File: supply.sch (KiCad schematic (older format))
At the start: 35 parts

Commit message: - battery charger develop - added sheet (every sheet contains total number of sheets, thats beacouse here are changes in all sheets)
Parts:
- removed C? (x6): 1u, symbol Device:C_Small
- removed D? (x2): D_Small, symbol Device:D_Small
- added C? (x6): 1u, Capacitor_SMD:C_0603_1608Metric_Pad1.05x0.95mm_HandSolder, symbol Device:C_Small
- added C? (x4): 2u2, Capacitor_SMD:C_0805_2012Metric_Pad1.15x1.40mm_HandSolder, symbol Device:C_Small
- added D? (x2): PMEG4005EJ, Diode_SMD:D_SOD-323F, symbol Diode:PMEG4005EJ
- added D?: Green, Diode_SMD:D_0805_2012Metric_Pad1.15x1.40mm_HandSolder, symbol Device:LED_Small
- added D?: Red, Diode_SMD:D_0805_2012Metric_Pad1.15x1.40mm_HandSolder, symbol Device:LED_Small
- added NTC?: 10k, Resistor_THT:R_Axial_DIN0204_L3.6mm_D1.6mm_P2.54mm_Vertical, symbol Device:Thermistor_NTC
- added Q?: BC807, Package_TO_SOT_SMD:SOT-23, symbol Transistor_BJT:BC807
- added Q?: BC817, Package_TO_SOT_SMD:SOT-23, symbol Device:Q_NPN_BCE
- added Q? (x2): BSS138, Package_TO_SOT_SMD:SOT-23, symbol Transistor_FET:BSS138
- added R?: 10k, Resistor_SMD:R_0603_1608Metric_Pad1.05x0.95mm_HandSolder, symbol Device:R_Small
- added R? (x4): 47k, Resistor_SMD:R_0603_1608Metric_Pad1.05x0.95mm_HandSolder, symbol Device:R_Small
- added R?: 1k3, Resistor_SMD:R_0603_1608Metric_Pad1.05x0.95mm_HandSolder, symbol Device:R_Small
- added R?: 890R, Resistor_SMD:R_0603_1608Metric_Pad1.05x0.95mm_HandSolder, symbol Device:R_Small
- added R? (x3): 1k, Resistor_SMD:R_0603_1608Metric_Pad1.05x0.95mm_HandSolder, symbol Device:R_Small
- added SW?: SW_DIP_x02, Button_Switch_SMD:SW_DIP_SPSTx02_Slide_6.7x6.64mm_W8.61mm_P2.54mm_LowProfile, symbol Switch:SW_DIP_x02
- added SW?: PWRON, symbol Switch:SW_MEC_5E
- C? (x4): footprint (none) -> Capacitor_SMD:C_0603_1608Metric_Pad1.05x0.95mm_HandSolder
- D?: footprint (none) -> Diode_SMD:D_0805_2012Metric_Pad1.15x1.40mm_HandSolder
- R? (x8): footprint (none) -> Resistor_SMD:R_0603_1608Metric_Pad1.05x0.95mm_HandSolder
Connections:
- net labels added: PWRON_MCU, SYSOFF, Vusb
- wire segments 77 -> 136
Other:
- note added: "PMEG4005 - Ir = 8 uA, surge 10 A\nCd = 43 pF - that is, @12V 500 kHz -> W = 6.2nJ, P = 3 mW\nPMEG4005EJ - 5 Aavg"
- moved on the sheet: BT?, C?, D?, J?, R?, U?

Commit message: - supply converter develop - added sheet: MCU - cleanup 'koncepcja' sub-schematics
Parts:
- removed BT?: Battery_Cell, symbol Device:Battery_Cell
- removed C? (x6): 1u, Capacitor_SMD:C_0603_1608Metric_Pad1.05x0.95mm_HandSolder, symbol Device:C_Small
- removed C? (x4): 2u2, Capacitor_SMD:C_0805_2012Metric_Pad1.15x1.40mm_HandSolder, symbol Device:C_Small
- removed D?: Orange, Diode_SMD:D_0805_2012Metric_Pad1.15x1.40mm_HandSolder, symbol Device:LED_Small
- removed D?: Green, Diode_SMD:D_0805_2012Metric_Pad1.15x1.40mm_HandSolder, symbol Device:LED_Small
- removed D?: Red, Diode_SMD:D_0805_2012Metric_Pad1.15x1.40mm_HandSolder, symbol Device:LED_Small
- removed J?: USB_B_Micro, Connector_USB:USB_Micro-B_Amphenol_10103594-0001LF_Horizontal, symbol Connector:USB_B_Micro
- removed NTC?: 10k, Resistor_THT:R_Axial_DIN0204_L3.6mm_D1.6mm_P2.54mm_Vertical, symbol Device:Thermistor_NTC
- removed Q? (x2): SI2365EDS, Package_TO_SOT_SMD:SOT-23, symbol Device:Q_PMOS_GDS
- removed Q? (x2): BC817, Package_TO_SOT_SMD:SOT-23, symbol Device:Q_NPN_BCE
- removed Q?: BC807, Package_TO_SOT_SMD:SOT-23, symbol Transistor_BJT:BC807
- removed Q? (x2): BSS138, Package_TO_SOT_SMD:SOT-23, symbol Transistor_FET:BSS138
- removed R? (x3): 10k, Resistor_SMD:R_0603_1608Metric_Pad1.05x0.95mm_HandSolder, symbol Device:R_Small
- removed R? (x5): 1k, Resistor_SMD:R_0603_1608Metric_Pad1.05x0.95mm_HandSolder, symbol Device:R_Small
- removed R? (x4): 47k, Resistor_SMD:R_0603_1608Metric_Pad1.05x0.95mm_HandSolder, symbol Device:R_Small
- removed R?: 1k3, Resistor_SMD:R_0603_1608Metric_Pad1.05x0.95mm_HandSolder, symbol Device:R_Small
- removed R?: 890R, Resistor_SMD:R_0603_1608Metric_Pad1.05x0.95mm_HandSolder, symbol Device:R_Small
- removed SW?: SW_DIP_x02, Button_Switch_SMD:SW_DIP_SPSTx02_Slide_6.7x6.64mm_W8.61mm_P2.54mm_LowProfile, symbol Switch:SW_DIP_x02
- removed SW?: PWRON, symbol Switch:SW_MEC_5E
- removed U?: BQ24079RGT, Package_DFN_QFN:VQFN-16-1EP_3x3mm_P0.5mm_EP1.6x1.6mm, symbol Battery_Management:BQ24079RGT
- added C? (x5): 2u2, Capacitor_SMD:C_0805_2012Metric_Pad1.15x1.40mm_HandSolder, symbol Device:C_Small
- added C? (x5): 1u, Capacitor_SMD:C_0603_1608Metric_Pad1.05x0.95mm_HandSolder, symbol Device:C_Small
- added C?: 1u, Capacitor_SMD:C_0805_2012Metric_Pad1.15x1.40mm_HandSolder, symbol Device:C_Small
- added C? (x6): 100n, Capacitor_SMD:C_0603_1608Metric_Pad1.05x0.95mm_HandSolder, symbol Device:C_Small
- added D? (x2): PMEG4005EJ, Diode_SMD:D_SOD-323F, symbol Diode:PMEG4005EJ
- added D? (x4): 1N4448, Diode_SMD:D_SOD-323_HandSoldering, symbol Device:D_Small
- added R?: 1R, Resistor_SMD:R_0603_1608Metric_Pad1.05x0.95mm_HandSolder, symbol Device:R_Small
- added U?: L78L05_SO8, Package_SO:SOIC-8_3.9x4.9mm_P1.27mm, symbol Regulator_Linear:L78L05_SO8
- added U?: L79L05_SO8, Package_SO:SOIC-8_3.9x4.9mm_P1.27mm, symbol Regulator_Linear:L79L05_SO8
- C?: footprint Capacitor_SMD:C_0603_1608Metric_Pad1.05x0.95mm_HandSolder -> Capacitor_SMD:C_0805_2012Metric_Pad1.15x1.40mm_HandSolder
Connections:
- net labels added: +5V, -5V, BATT_IN
- net labels removed: +BATT, HV_EN, PWRON_MCU, SYSOFF, Vusb
- wire segments 136 -> 98
- no-connect marks 3 -> 0
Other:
- note added: "PMEG4005 - Ir = 8 uA, surge 10 A\nCd = 43 pF - that is, @12V 500 kHz -> W = 6.2nJ, P = 3 mW\n\nPMEG4005EJ - 5 Aavg"
- note removed: "PMEG4005 - Ir = 8 uA, surge 10 A\nCd = 43 pF - that is, @12V 500 kHz -> W = 6.2nJ, P = 3 mW\nPMEG4005EJ - 5 Aavg"
- moved on the sheet: C?, D?, L?, R?

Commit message: - added footprint & 3D model of DC/DC HV converter - updated battery (to 2x battery holder) - some changes in supply
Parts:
- removed C?: 2u2, Capacitor_SMD:C_0805_2012Metric_Pad1.15x1.40mm_HandSolder, symbol Device:C_Small
- removed C?: 100n, Capacitor_SMD:C_0603_1608Metric_Pad1.05x0.95mm_HandSolder, symbol Device:C_Small
- removed C? (x3): 1u, Capacitor_SMD:C_0603_1608Metric_Pad1.05x0.95mm_HandSolder, symbol Device:C_Small
- removed D? (x3): 1N4448, Diode_SMD:D_SOD-323_HandSoldering, symbol Device:D_Small
- removed D? (x4): PMEG4005EJ, Diode_SMD:D_SOD-323F, symbol Diode:PMEG4005EJ
- removed U?: L78L15_SO8, Package_SO:SOIC-8_3.9x4.9mm_P1.27mm, symbol Regulator_Linear:L78L15_SO8
- removed U?: PAM242x, Package_SO:SOIC-8-1EP_3.9x4.9mm_P1.27mm_EP2.29x3mm_ThermalVias, symbol Diotec:PAM242x
- removed U?: L78L05_SO8, Package_SO:SOIC-8_3.9x4.9mm_P1.27mm, symbol Regulator_Linear:L78L05_SO8
- removed U?: L79L05_SO8, Package_SO:SOIC-8_3.9x4.9mm_P1.27mm, symbol Regulator_Linear:L79L05_SO8
- added C? (x3): 1u, Capacitor_SMD:C_0603_1608Metric_Pad1.05x0.95mm_HandSolder, symbol Device:C_Small
- added C?: 1u, Capacitor_SMD:C_0805_2012Metric_Pad1.15x1.40mm_HandSolder, symbol Device:C_Small
- added C?: 2u2, Capacitor_SMD:C_0805_2012Metric_Pad1.15x1.40mm_HandSolder, symbol Device:C_Small
- added C? (x2): 100n, Capacitor_SMD:C_0603_1608Metric_Pad1.05x0.95mm_HandSolder, symbol Device:C_Small
- added C?: 1n, Capacitor_SMD:C_0805_2012Metric_Pad1.15x1.40mm_HandSolder, symbol Device:C_Small
- added C? (x4): 10u, Capacitor_SMD:C_0805_2012Metric_Pad1.15x1.40mm_HandSolder, symbol Device:C_Small
- added D?: 1N4448, Diode_SMD:D_SOD-323_HandSoldering, symbol Device:D_Small
- added D? (x6): PMEG4005EJ, Diode_SMD:D_SOD-323_HandSoldering, symbol Diode:PMEG4005EJ
- added D?: PMEG4005EJ, Diode_SMD:D_SOD-123F, symbol Diode:PMEG4005EJ
- added L?: 2u2, Inductor_SMD:L_1008_2520Metric, symbol Device:L_Core_Ferrite
- added R?: 13k2, Resistor_SMD:R_0603_1608Metric_Pad1.05x0.95mm_HandSolder, symbol Device:R_Small
- added R? (x2): 1k2, Resistor_SMD:R_0603_1608Metric_Pad1.05x0.95mm_HandSolder, symbol Device:R_Small
- added R?: 1R, Resistor_SMD:R_0603_1608Metric_Pad1.05x0.95mm_HandSolder, symbol Device:R_Small
- added R?: 3k6, Resistor_SMD:R_0603_1608Metric_Pad1.05x0.95mm_HandSolder, symbol Device:R_Small
- added R?: 5R, Resistor_SMD:R_0603_1608Metric_Pad1.05x0.95mm_HandSolder, symbol Device:R_Small
- added U?: LM317L_SOT89, Package_TO_SOT_SMD:SOT-89-3, symbol Regulator_Linear:LM317L_SOT-89
- added U?: PAM242x, symbol DiodesInc:PAM242x
- added U?: LM337L_SO8, Package_SO:SOIC-8_3.9x4.9mm_P1.27mm, symbol Regulator_Linear:LM337L_SO8
- added U?: TPS613222ADBV, Package_TO_SOT_SMD:SOT-23-5, symbol Regulator_Switching:TPS613222ADBV
- D?: value PMEG60T50 -> PMEG3050BEP
- R?: value 10k -> 1k
- R?: value 85k -> 8k5
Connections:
- wire segments 98 -> 136
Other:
- note added: "PMEG4005 - Ir = 8 uA, surge 10 A\nCd = 43 pF - that is, @12V 500 kHz -> W = 6.2nJ, P = 3 mW\n\nPMEG4005EJ - 5 Aavg\n\n5 V line current: ca. 100-150 mA\n\nLM317/LM337 was used instead fixed LDO's beacouse of lower Iq (bias) current."
- note added: "Recommended 3x GRM188R60J106ME84D\n0603 10 uF 6.3V X5R 20% MLCC\n\nSnubber: C must be >3x diode capacitance"
- note removed: "PMEG4005 - Ir = 8 uA, surge 10 A\nCd = 43 pF - that is, @12V 500 kHz -> W = 6.2nJ, P = 3 mW\n\nPMEG4005EJ - 5 Aavg"
- moved on the sheet: C?, D?, R?

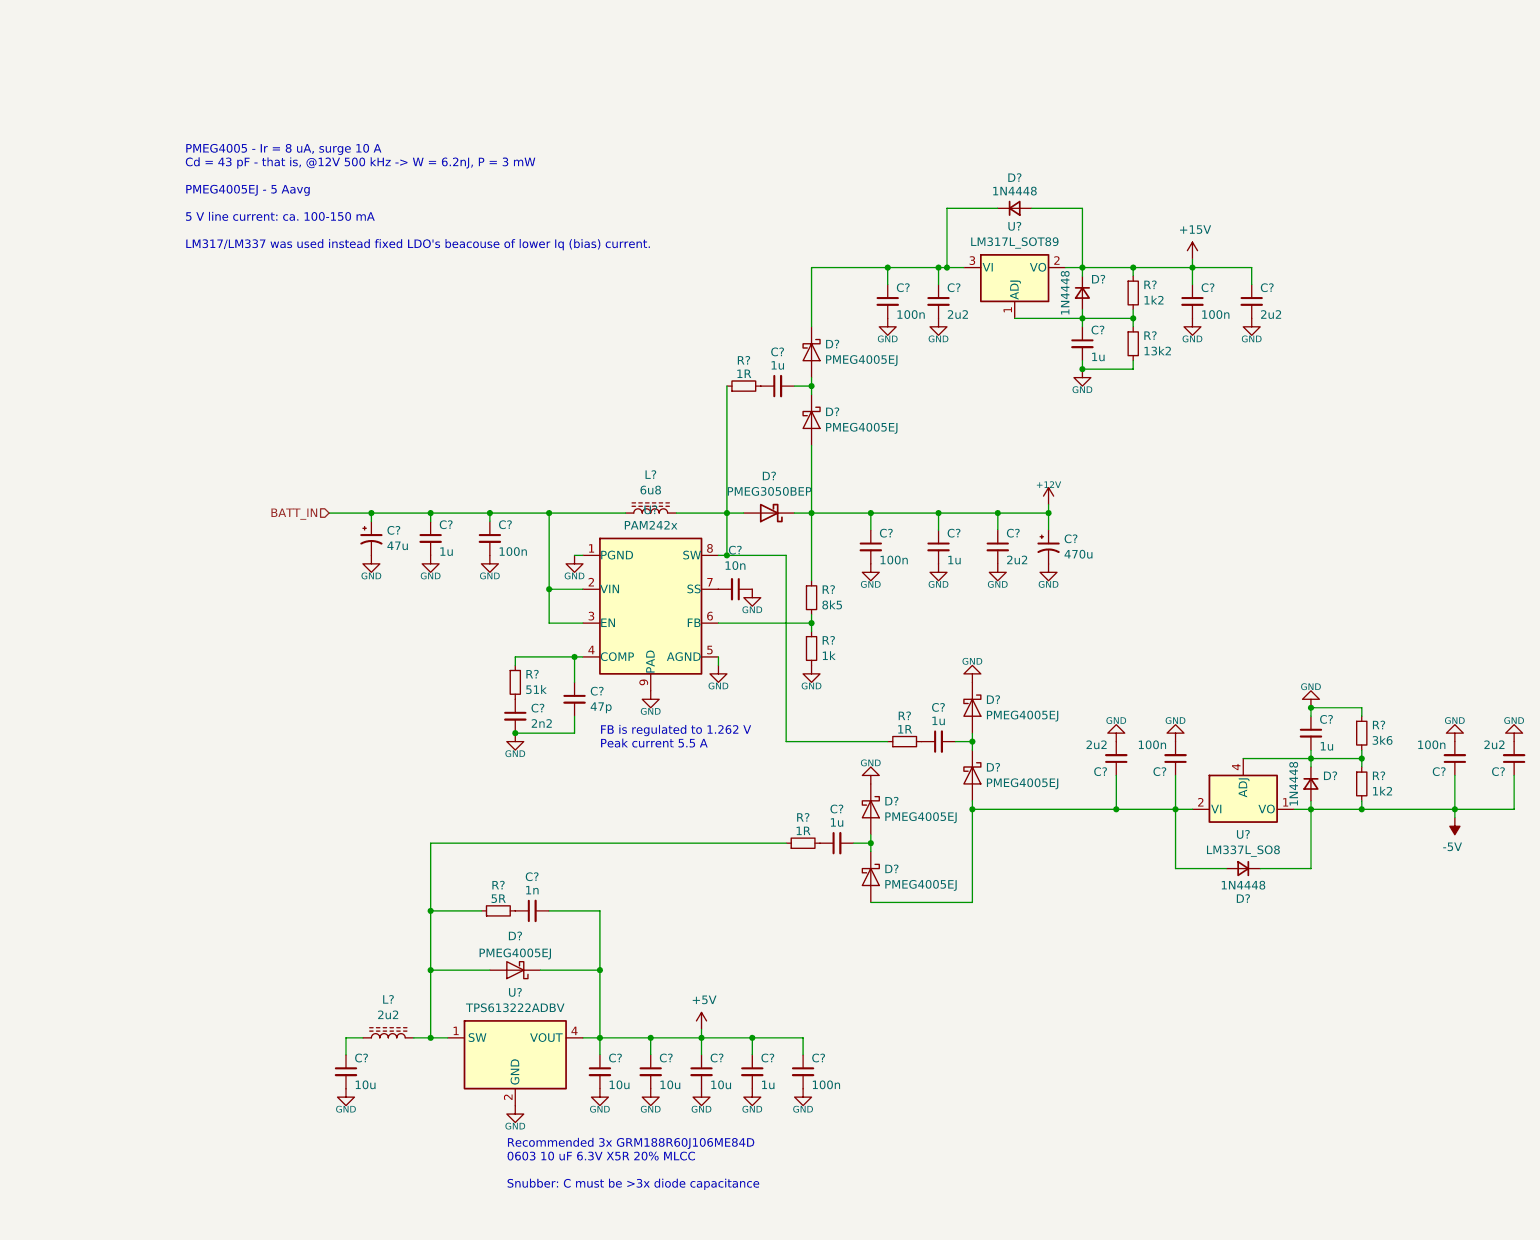
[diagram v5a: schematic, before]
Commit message: - drivers modified - MCU replaced
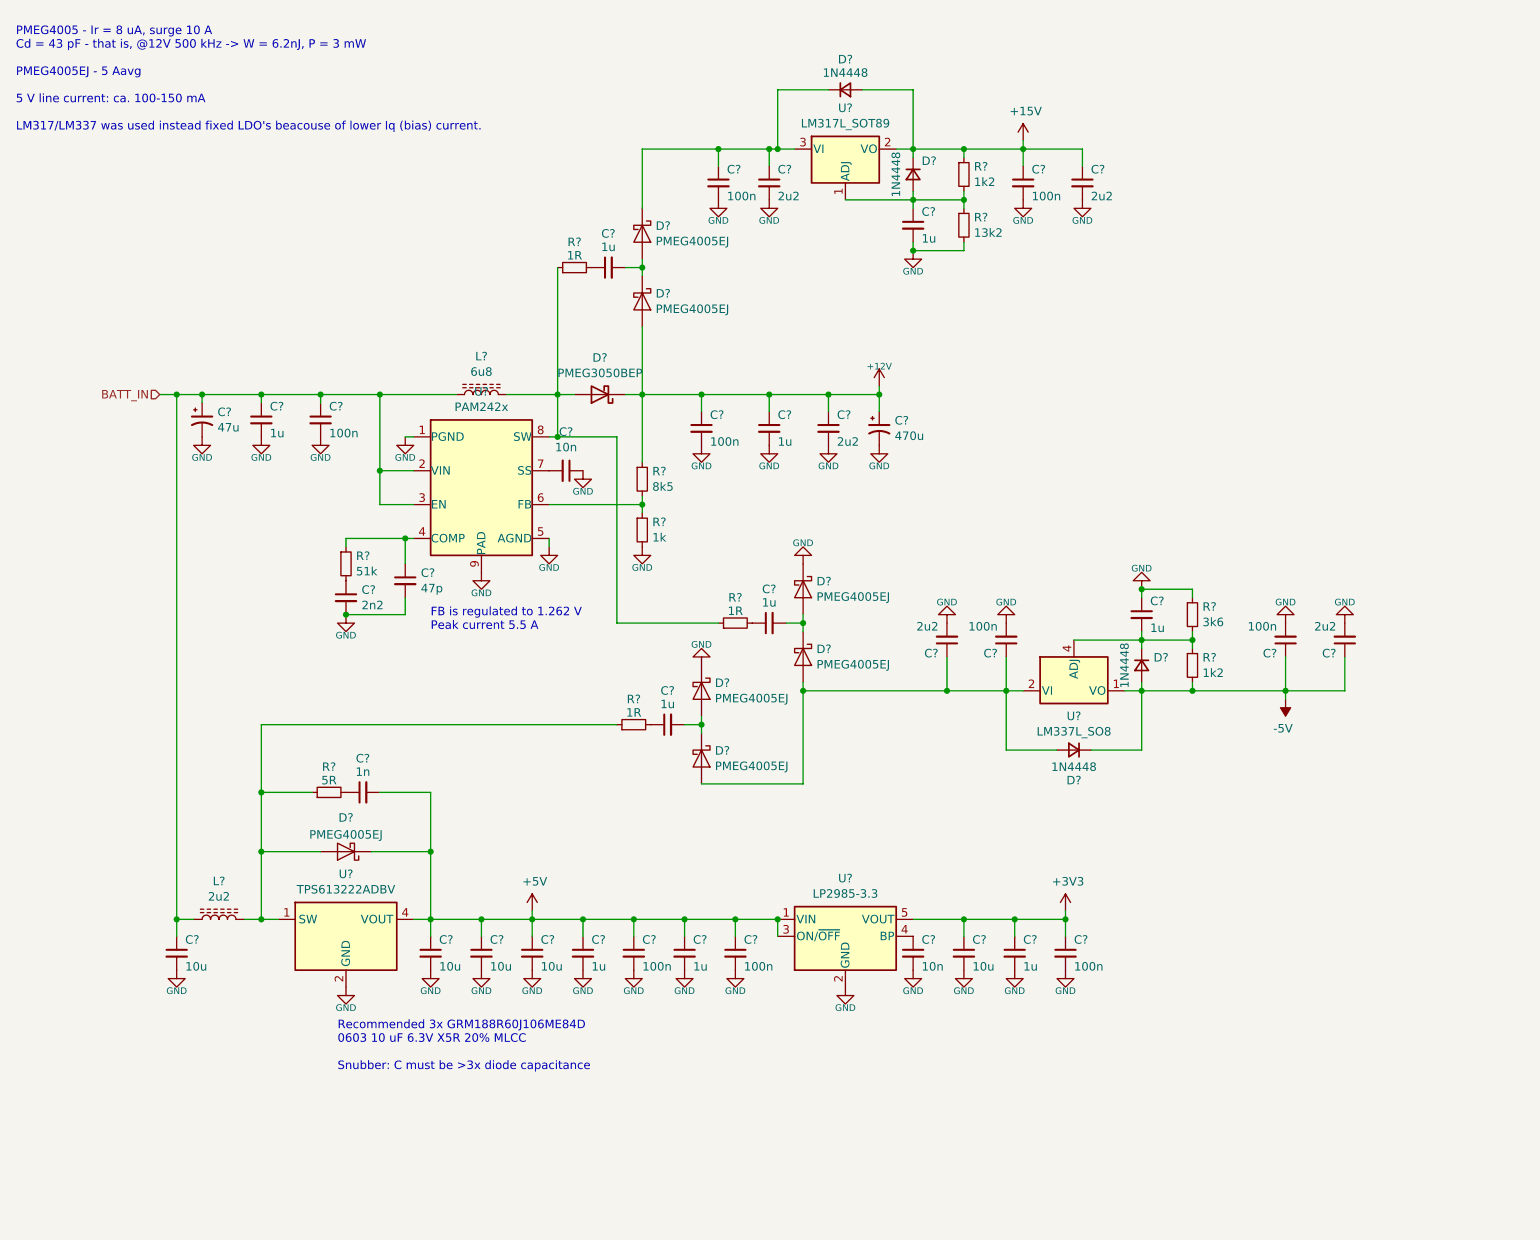
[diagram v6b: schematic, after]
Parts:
- added C?: 10n, Capacitor_SMD:C_0603_1608Metric_Pad1.05x0.95mm_HandSolder, symbol Device:C_Small
- added C? (x2): 100n, Capacitor_SMD:C_0603_1608Metric_Pad1.05x0.95mm_HandSolder, symbol Device:C_Small
- added C? (x2): 1u, Capacitor_SMD:C_0603_1608Metric_Pad1.05x0.95mm_HandSolder, symbol Device:C_Small
- added C?: 10u, Capacitor_SMD:C_0805_2012Metric_Pad1.15x1.40mm_HandSolder, symbol Device:C_Small
- added U?: LP2985-3.3, Package_TO_SOT_SMD:SOT-23-5, symbol Regulator_Linear:LP2985-3.3
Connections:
- net +5V: now also C?.1, C?.1, U?.1 (VIN), U?.3 (ON/~OFF~)
- net BATT_IN: now also C?.1, L?.1
- net GND: now also C?.2, C?.2, C?.2, C?.2, C?.2, C?.2, U?.2 (GND)
- new net: C?.1, U?.4 (BP)
- new net +3V3: C?.1, C?.1, C?.1, U?.5 (VOUT)
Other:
- moved on the sheet: C?, D?, L?, R?, U?

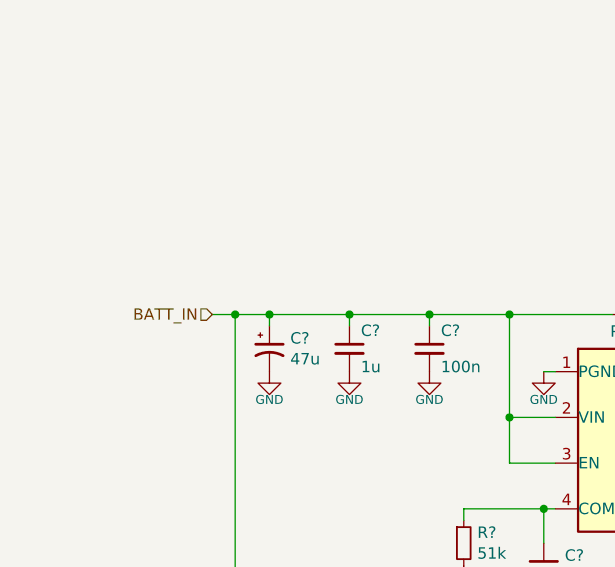
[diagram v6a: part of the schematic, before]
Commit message: - connect things to MCUlow (DAC, screen, keys, debug) - improvement in charger (read PWR key)
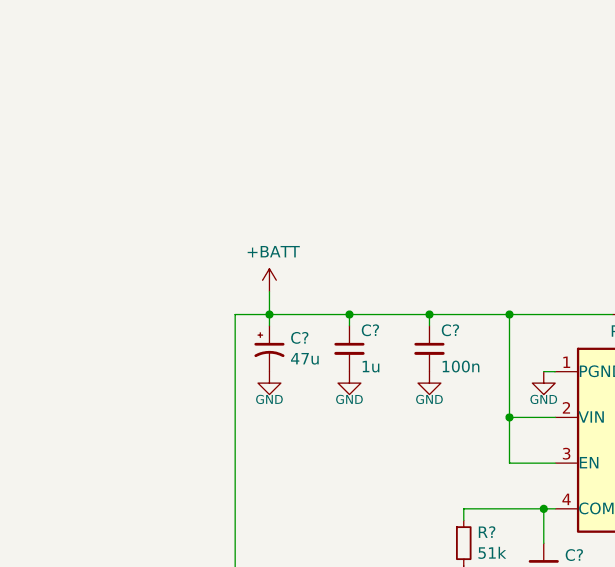
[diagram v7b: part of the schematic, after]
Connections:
- net BATT_IN renamed +BATT
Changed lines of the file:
@@
 	0    -1   -1   0
 $EndComp
-Text HLabel 1500 2800 0    50   Input ~ 0
-BATT_IN
 Wire Wire Line
 	4700 2800 5100 2800
@@
 Wire Wire Line
 	5450 2800 5750 2800
-Wire Wire Line
-	1500 2800 1600 2800
 $Comp
 L Device:R_Small R?
@@
 	1600 5900 1600 2800
 Connection ~ 1600 5900
-Connection ~ 1600 2800
 Wire Wire Line
 	1600 2800 1750 2800
@@
 	6850 5900 6850 5850
 Connection ~ 6850 5900
+$Comp
+L power:+BATT #PWR?
+U 1 1 60010109
+P 1750 2700
+AR Path="/5F620813/60010109" Ref="#PWR?"  Part="1"
+AR Path="/5F7A93EE/60010109" Ref="#PWR?"  Part="1"
+F 0 "#PWR?" H 1750 2550 50  0001 C CNN
+F 1 "+BATT" H 1765 2873 50  0000 C CNN
+F 2 "" H 1750 2700 50  0001 C CNN
+F 3 "" H 1750 2700 50  0001 C CNN
+	1    1750 2700
+	1    0    0    -1
+$EndComp
+Wire Wire Line
+	1750 2700 1750 2800
 $EndSCHEMATC
